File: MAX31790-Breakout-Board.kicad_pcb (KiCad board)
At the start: 2 copper layers, 55.9 x 58.4 mm, 26 parts, among them J1 Conn_01x07, J2 Conn_01x05, J3 Screw_Terminal_01x02, M1 Fan_4pin, M2 Fan_4pin, M3 Fan_4pin, M4 Fan_4pin, M5 Fan_4pin, M6 Fan_4pin, U1 MAX31790ATI_T

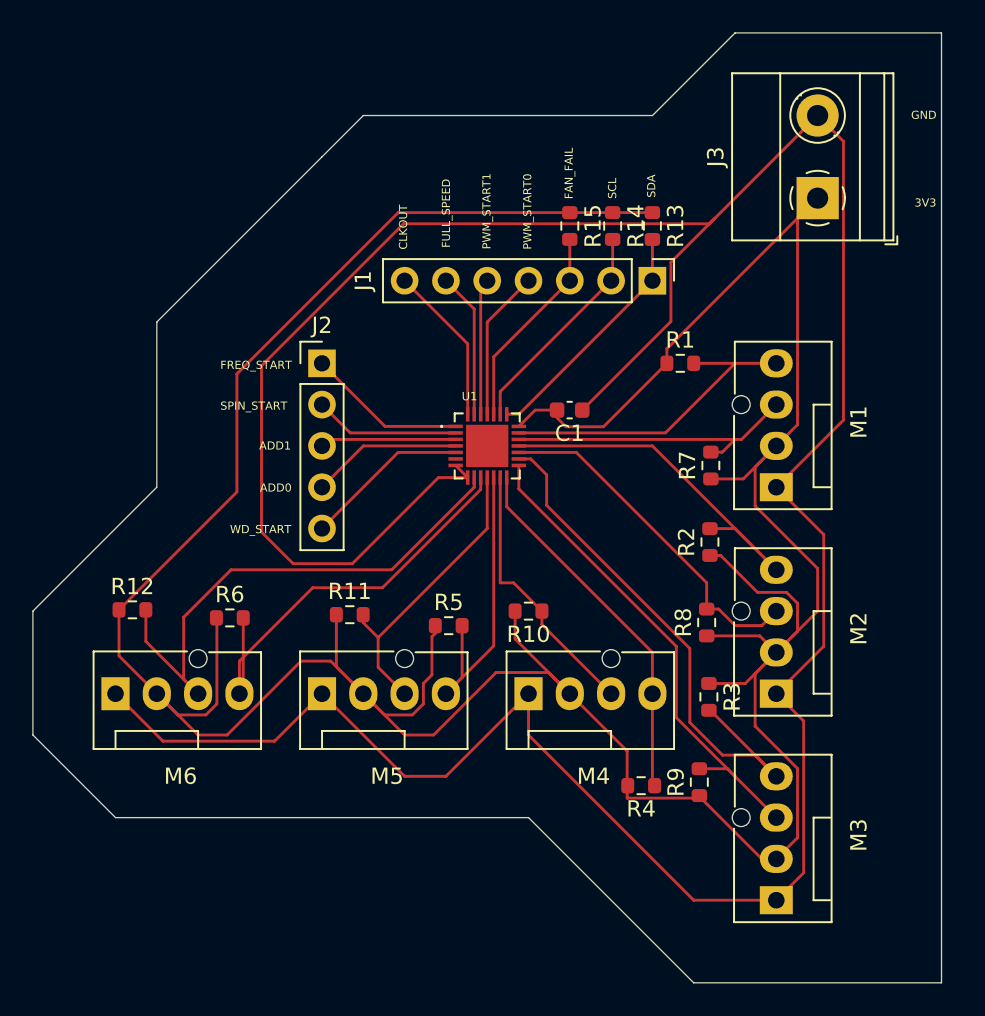
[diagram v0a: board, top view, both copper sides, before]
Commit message: Added +12V line for fan power
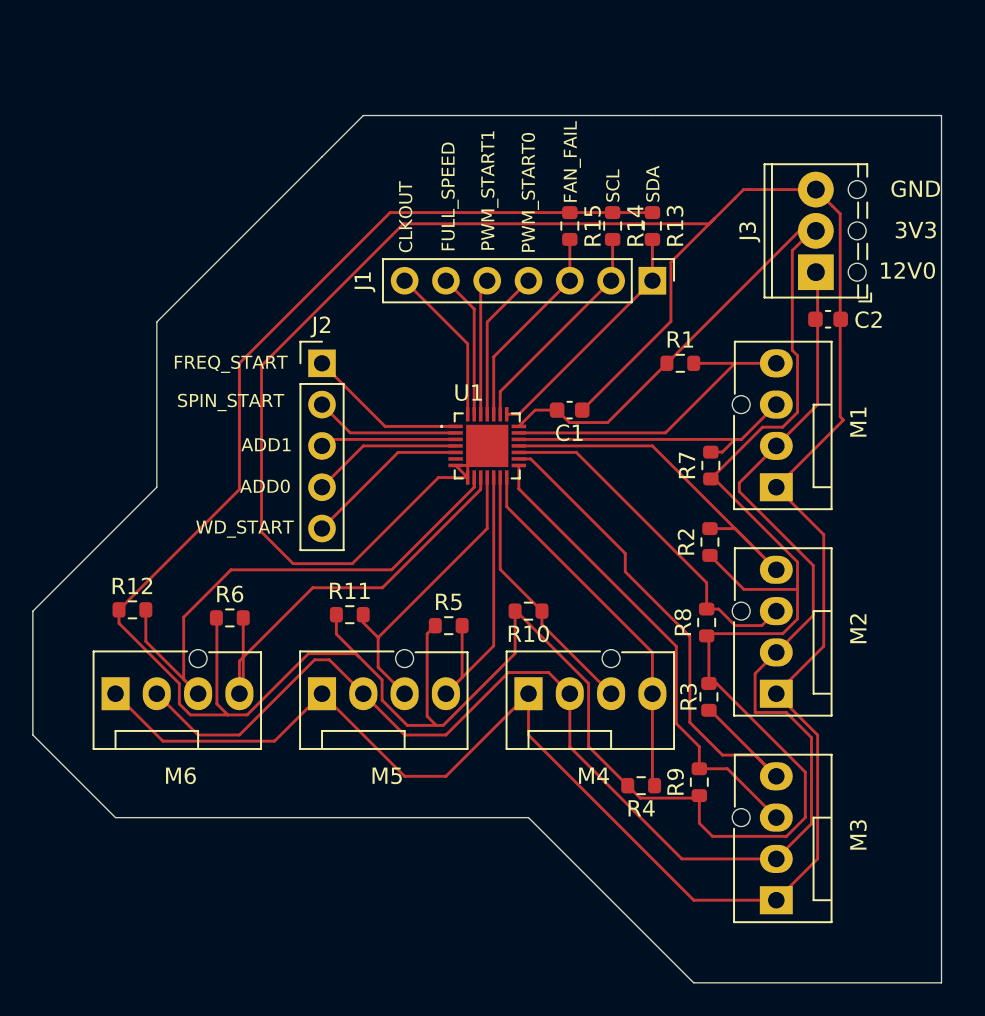
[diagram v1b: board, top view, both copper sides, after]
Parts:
- added C2: 1uF, Capacitor_SMD:C_0603_1608Metric, F.Cu at (155.6, 73.5)
- J3: value Screw_Terminal_01x02 -> Screw_Terminal_01x03; footprint TerminalBlock_Phoenix:TerminalBlock_Phoenix_MKDS-1,5-2-5.08_1x02_P5.08mm_Horizontal -> TerminalBlock_Phoenix:TerminalBlock_Phoenix_MPT-0,5-3-2.54_1x03_P2.54mm_Horizontal
- moved J3 4.56 mm to (154.8, 70.6)
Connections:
- J3 pad 1: +3V3 -> +12V
- J3 pad 2: GND -> +3V3
- M1 pad 2: +3V3 -> +12V
- M2 pad 2: +3V3 -> +12V
- M3 pad 2: +3V3 -> +12V
- M4 pad 2: +3V3 -> +12V
- M5 pad 2: +3V3 -> +12V
- M6 pad 2: +3V3 -> +12V
- U1 pad 29: unconnected-(U1-EXPPAD-Pad29) -> GND
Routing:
- net +12V: track 0.00 -> 96.2 mm
- net +3V3: track 233.4 -> 207.9 mm
- net GND: track 191.1 -> 188.5 mm
- net /TACH3: track 30.6 -> 29.2 mm
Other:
- board size 55.9 x 58.4 mm -> 55.9 x 53.3 mm
- board text added: "12V0"

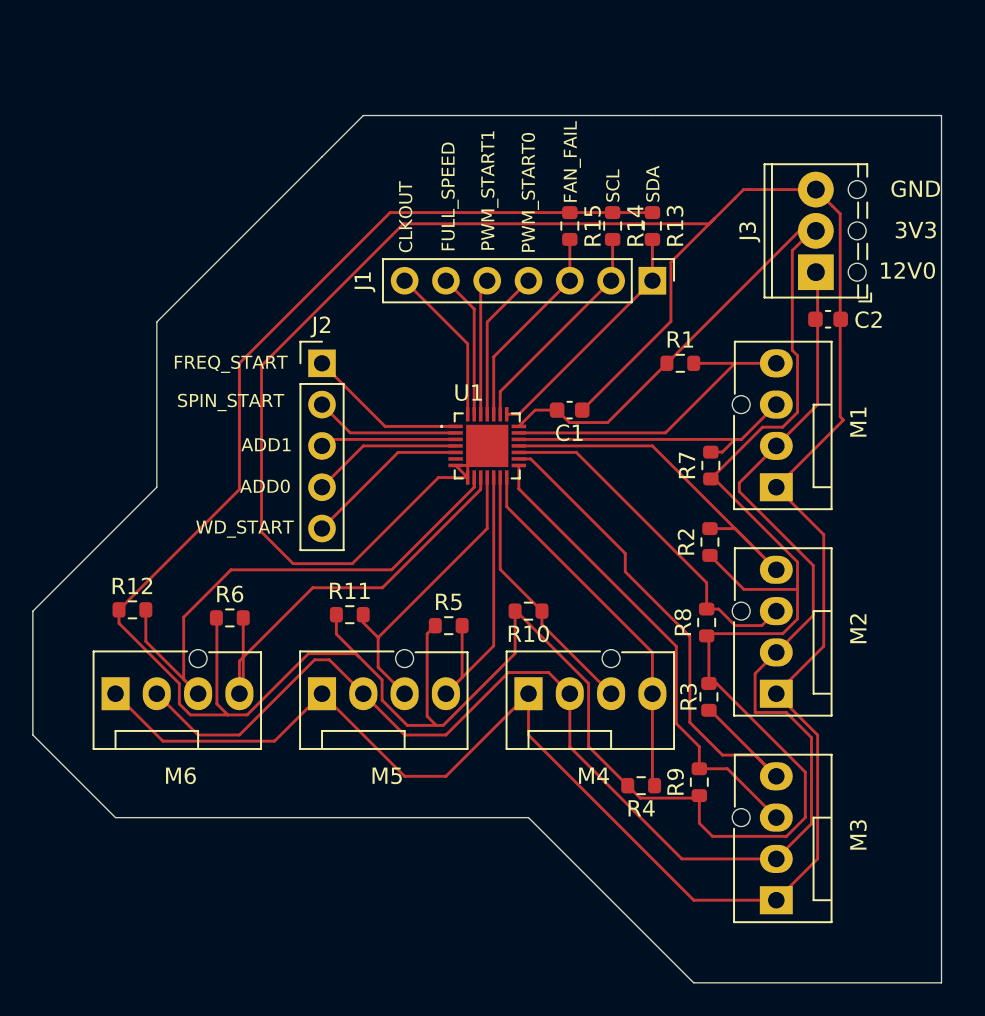
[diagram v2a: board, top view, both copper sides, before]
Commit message: Added ground plane, increased +12v track width
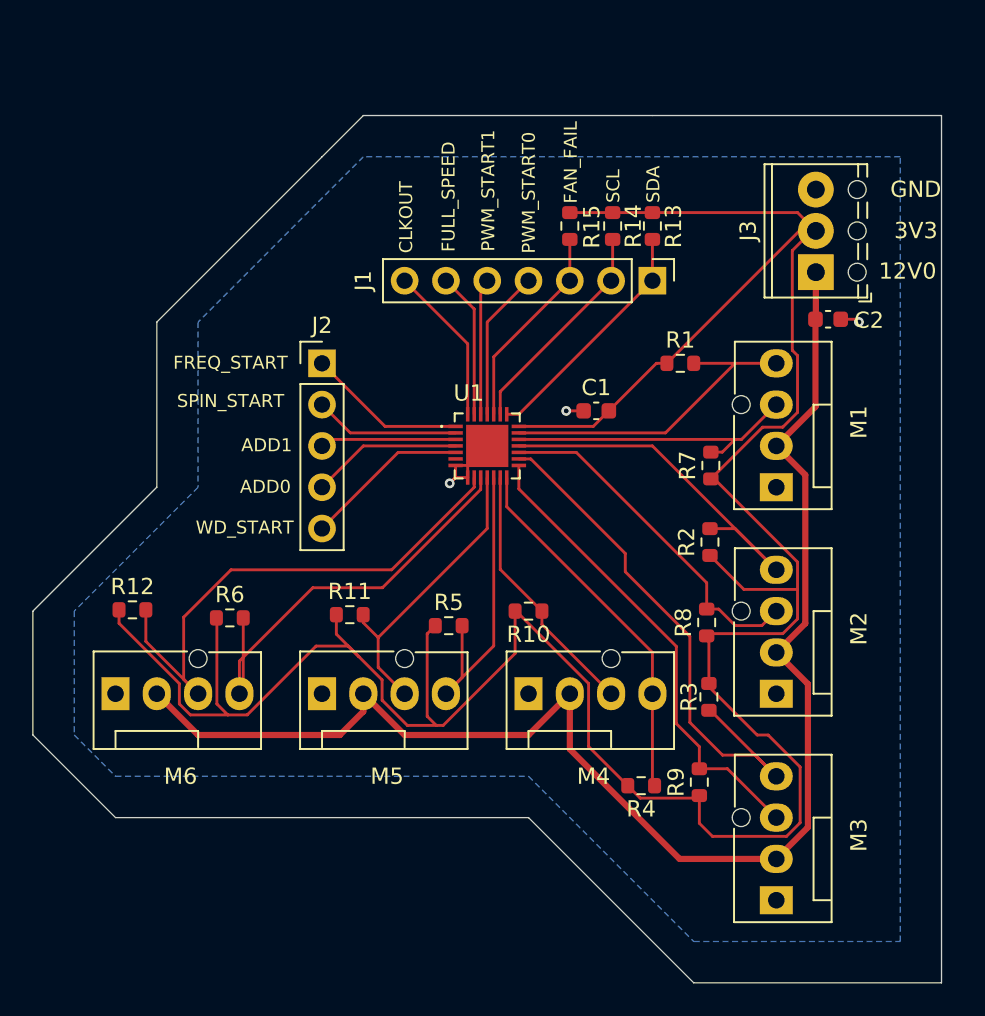
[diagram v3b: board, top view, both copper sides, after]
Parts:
- moved C1 1.63 mm to (141.3, 79.1), turned to 0 degrees
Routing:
- net GND: track 188.5 -> 7.96 mm, vias 0 -> 3
- net +3V3: track 207.9 -> 175.6 mm
- net +12V: track 96.2 -> 89.3 mm
- added copper zone on B.Cu, net GND
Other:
- rule pad_to_mask_clearance: 0 -> 0.038
